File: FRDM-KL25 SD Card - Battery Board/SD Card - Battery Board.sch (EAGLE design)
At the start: 16 parts, among them U1 TPS63001, U2 TPS63002

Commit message: FRDM-KL25Z: Changed library used for passives
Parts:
- R1, R2, R3, R4, R5, R6, R7, R8: device Kas-Passives:RESISTOR10K-62.5M-1%-50V -> Kas-Resistors:RESISTOR10K-62.5M-1%-50V
- R10, R9: device Kas-Passives:RESISTOR0402 -> Kas-Resistors:RESISTOR200-100M-1%-50V
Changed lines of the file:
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@@
 <part name="U$1" library="Kas-Connectors" deviceset="693061010991" device=""/>
 <part name="C1" library="Kas-Passives" deviceset="CAPACITOR" device="1U-X5R-10%-10V" value="1 uF"/>
-<part name="R1" library="Kas-Passives" deviceset="RESISTOR" device="10K-62.5M-1%-50V" value="10k"/>
-<part name="R2" library="Kas-Passives" deviceset="RESISTOR" device="10K-62.5M-1%-50V" value="10k"/>
-<part name="R3" library="Kas-Passives" deviceset="RESISTOR" device="10K-62.5M-1%-50V" value="10k"/>
-<part name="R4" library="Kas-Passives" deviceset="RESISTOR" device="10K-62.5M-1%-50V" value="10k"/>
-<part name="R5" library="Kas-Passives" deviceset="RESISTOR" device="10K-62.5M-1%-50V" value="10k"/>
-<part name="R6" library="Kas-Passives" deviceset="RESISTOR" device="10K-62.5M-1%-50V" value="10k"/>
-<part name="R7" library="Kas-Passives" deviceset="RESISTOR" device="10K-62.5M-1%-50V" value="10k"/>
-<part name="R8" library="Kas-Passives" deviceset="RESISTOR" device="10K-62.5M-1%-50V" value="10k"/>
-<part name="R9" library="Kas-Passives" deviceset="RESISTOR" device="0402" value="200"/>
-<part name="R10" library="Kas-Passives" deviceset="RESISTOR" device="0402" value="200"/>
+<part name="R1" library="Kas-Resistors" deviceset="RESISTOR" device="10K-62.5M-1%-50V" value="10k"/>
+<part name="R2" library="Kas-Resistors" deviceset="RESISTOR" device="10K-62.5M-1%-50V" value="10k"/>
+<part name="R3" library="Kas-Resistors" deviceset="RESISTOR" device="10K-62.5M-1%-50V" value="10k"/>
+<part name="R4" library="Kas-Resistors" deviceset="RESISTOR" device="10K-62.5M-1%-50V" value="10k"/>
+<part name="R5" library="Kas-Resistors" deviceset="RESISTOR" device="10K-62.5M-1%-50V" value="10k"/>
+<part name="R6" library="Kas-Resistors" deviceset="RESISTOR" device="10K-62.5M-1%-50V" value="10k"/>
+<part name="R7" library="Kas-Resistors" deviceset="RESISTOR" device="10K-62.5M-1%-50V" value="10k"/>
+<part name="R8" library="Kas-Resistors" deviceset="RESISTOR" device="10K-62.5M-1%-50V" value="10k"/>
+<part name="R9" library="Kas-Resistors" deviceset="RESISTOR" device="200-100M-1%-50V" value="200"/>
+<part name="R10" library="Kas-Resistors" deviceset="RESISTOR" device="200-100M-1%-50V" value="200"/>
 <part name="U1" library="Kas-Buck Boost Battery Control" deviceset="TPS6300X" device="" value="TPS63001"/>
 <part name="U2" library="Kas-Buck Boost Battery Control" deviceset="TPS6300X" device="" value="TPS63002"/>

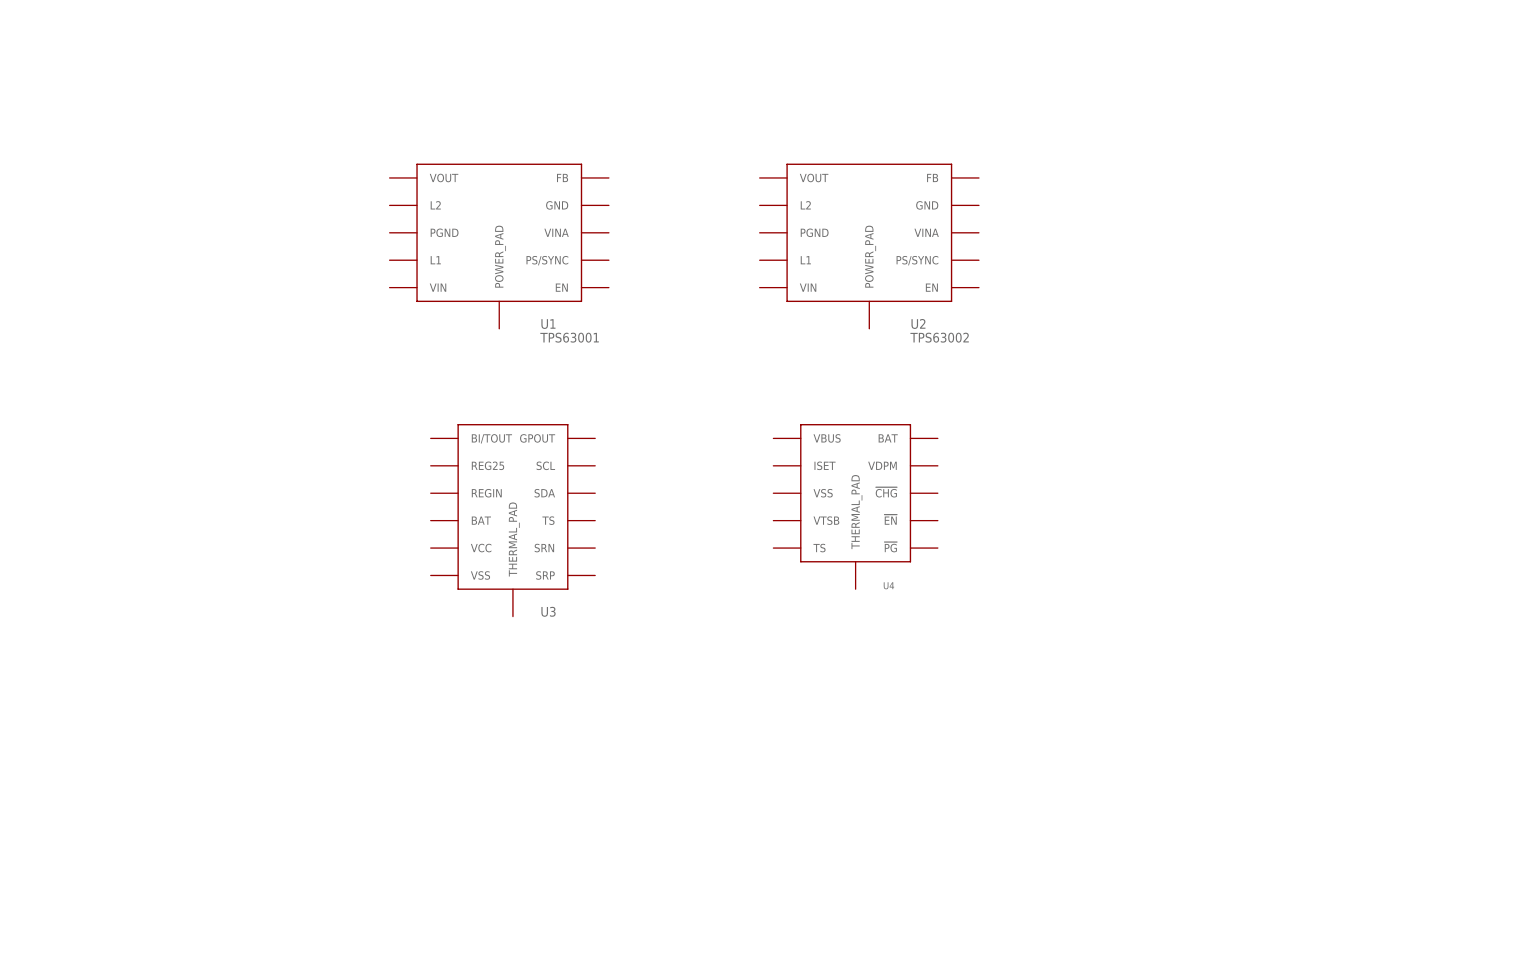
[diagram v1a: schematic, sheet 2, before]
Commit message: Removed .epf from version control, updated components
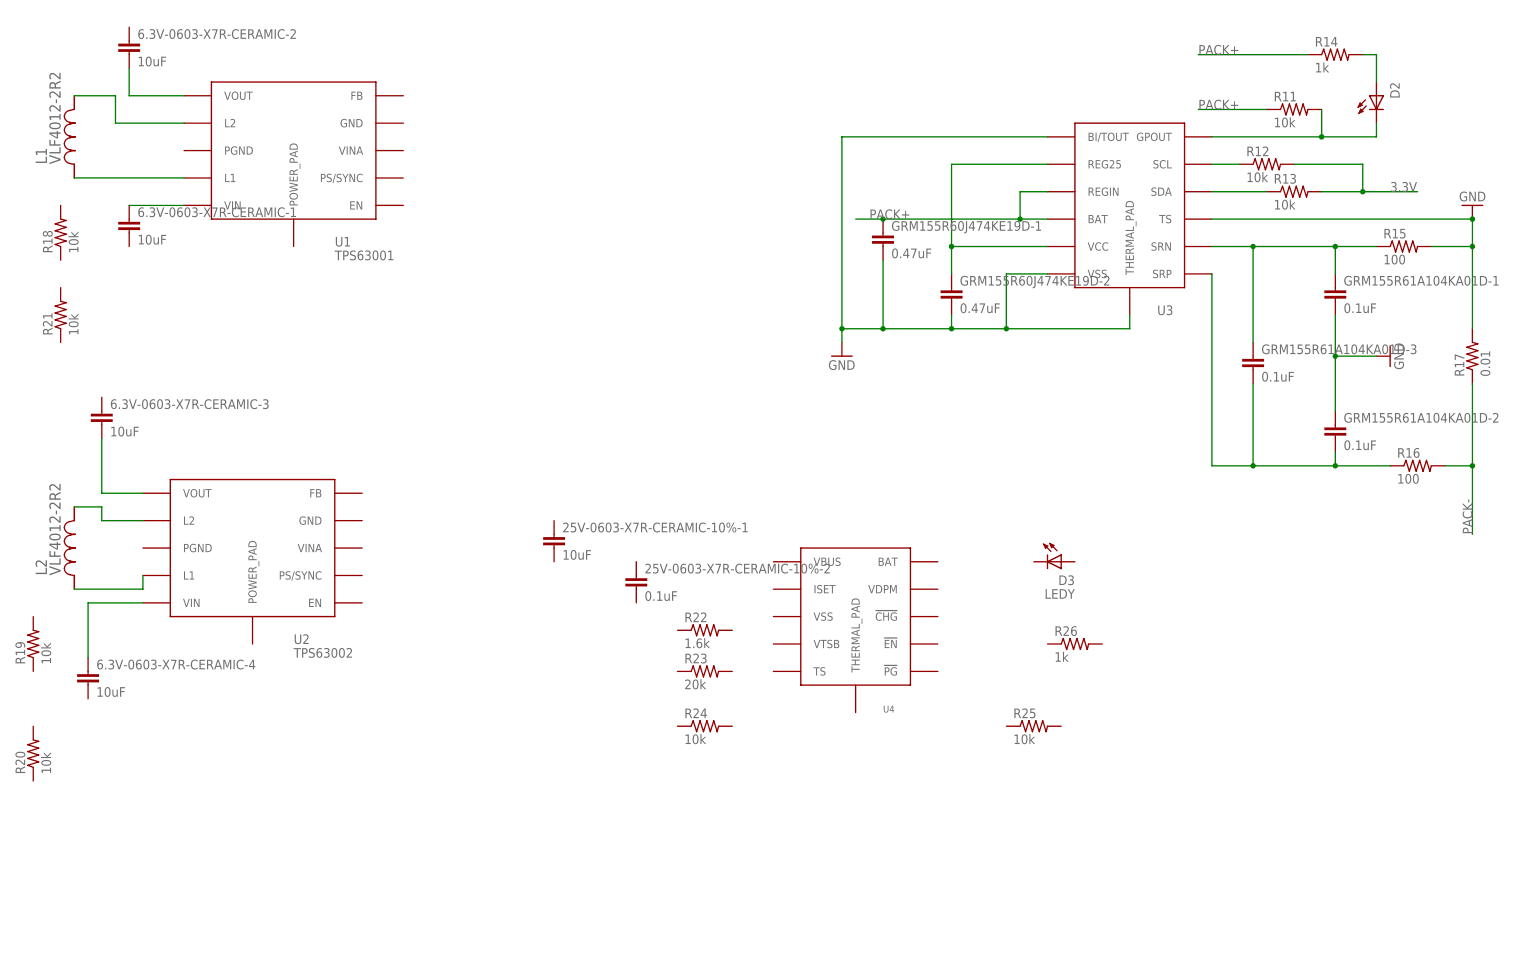
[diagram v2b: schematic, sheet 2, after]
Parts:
- removed U$1: 693061010991, Kas-Connectors:693061010991
- added 25V-0603-X7R-CERAMIC-10%-1, 6.3V-0603-X7R-CERAMIC-1, 6.3V-0603-X7R-CERAMIC-2, 6.3V-0603-X7R-CERAMIC-3, 6.3V-0603-X7R-CERAMIC-4: 10uF, Kas-Capacitors:CAPACITOR0603
- added 25V-0603-X7R-CERAMIC-10%-2, GRM155R61A104KA01D-1, GRM155R61A104KA01D-2, GRM155R61A104KA01D-3: 0.1uF, Kas-Capacitors:CAPACITOR0603
- added D2: (no value), Kas-Diodes-LEDs:LEDR
- added D3: LEDY, Kas-Diodes-LEDs:LEDG
- added GRM155R60J474KE19D-1, GRM155R60J474KE19D-2: 0.47uF, Kas-Capacitors:CAPACITOR0603
- added J1: (no value), Kas-Connectors:SD_CARD_SLOT
- added L1, L2: VLF4012-2R2, Kas-Inductors:XAL4020-222MEB
- added R11, R12, R13, R18, R19, R20, R21, R24, R25: 10k, Kas-Resistors:RESISTOR10K-62.5M-1%-50V
- added R14, R26: 1k, Kas-Resistors:RESISTOR0402
- added R15, R16: 100, Kas-Resistors:RESISTOR0402
- added R17: 0.01, Kas-Resistors:RESISTOR0402
- added R22: 1.6k, Kas-Resistors:RESISTOR0402
- added R23: 20k, Kas-Resistors:RESISTOR0402
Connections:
- new net 3.3V: R12.2, R13.2
- new net GND: GRM155R60J474KE19D-1.2, GRM155R60J474KE19D-2.2, GRM155R61A104KA01D-1.2, GRM155R61A104KA01D-2.1, R15.2, R17.2, U3.BI/TOUT, U3.THERMAL_PAD, U3.TS, U3.VSS
- new net N$1: GRM155R60J474KE19D-2.1, U3.REG25, U3.VCC
- new net N$10: 6.3V-0603-X7R-CERAMIC-1.1, U1.VIN
- new net N$11: 6.3V-0603-X7R-CERAMIC-2.2, U1.VOUT
- new net N$12: 6.3V-0603-X7R-CERAMIC-4.1, U2.VIN
- new net N$13: 6.3V-0603-X7R-CERAMIC-3.2, U2.VOUT
- new net N$14: L2.1, U2.L2
- new net N$15: L2.2, U2.L1
- new net N$2: R12.1, U3.SCL
- new net N$3: R13.1, U3.SDA
- new net N$4: D2.C, R11.2, U3.GPOUT
- new net N$5: D2.A, R14.2
- new net N$6: GRM155R61A104KA01D-2.2, GRM155R61A104KA01D-3.2, R16.1, U3.SRP
- new net N$7: GRM155R61A104KA01D-1.1, GRM155R61A104KA01D-3.1, R15.1, U3.SRN
- new net N$8: L1.1, U1.L2
- new net N$9: L1.2, U1.L1
- new net PACK+: GRM155R60J474KE19D-1.1, R11.1, R14.1, U3.BAT, U3.REGIN
- new net PACK-: R16.2, R17.1
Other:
- note added: "add schottky diode"
- moved on the sheet: U1, U2, U3, U4

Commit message: FRDM-KL25Z: Changed passives to use Newark approved parts
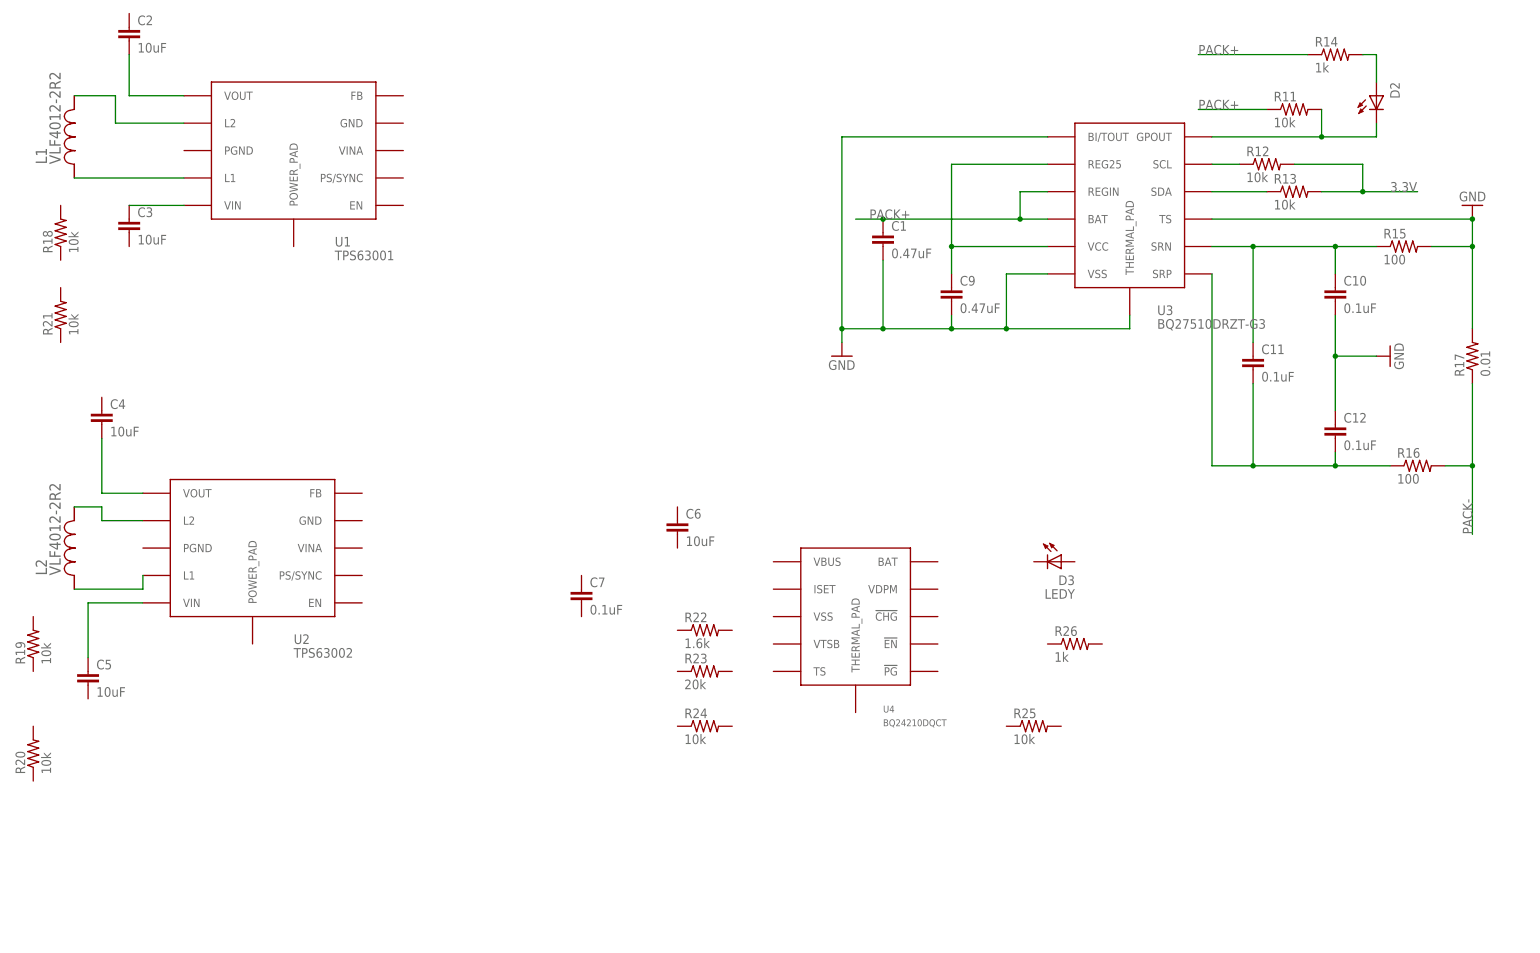
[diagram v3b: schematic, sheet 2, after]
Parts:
- removed 25V-0603-X7R-CERAMIC-10%-1, 6.3V-0603-X7R-CERAMIC-1, 6.3V-0603-X7R-CERAMIC-2, 6.3V-0603-X7R-CERAMIC-3, 6.3V-0603-X7R-CERAMIC-4: 10uF, Kas-Capacitors:CAPACITOR0603
- removed 25V-0603-X7R-CERAMIC-10%-2, GRM155R61A104KA01D-1, GRM155R61A104KA01D-2, GRM155R61A104KA01D-3: 0.1uF, Kas-Capacitors:CAPACITOR0603
- removed GRM155R60J474KE19D-1, GRM155R60J474KE19D-2: 0.47uF, Kas-Capacitors:CAPACITOR0603
- added C10, C11, C12, C7: 0.1uF, Kas-Capacitors:CAPACITOR0.1U-X5R-10%-10V-0402
- added C2, C3, C4, C5: 10uF, Kas-Capacitors:CAPACITOR10U-X7R-10%-6.3V
- added C6: 10uF, Kas-Capacitors:CAPACITOR10U-X7R-10%-25
- added C8: 1uF, Kas-Capacitors:CAPACITOR0.1U-X5R-10%-10V-0402
- added C9: 0.47uF, Kas-Capacitors:CAPACITOR0.1U-X5R-10%-10V-0402
- C1: value 1 uF -> 0.47uF; device Kas-Passives:CAPACITOR1U-X5R-10%-10V -> Kas-Capacitors:CAPACITOR0.1U-X5R-10%-10V-0402
- R10, R9: device Kas-Resistors:RESISTOR200-100M-1%-50V -> Kas-Resistors:RESISTOR0-100M-X%-50V
- R14, R15, R16, R17, R22, R23: device Kas-Resistors:RESISTOR0402 -> Kas-Resistors:RESISTOR0-100M-X%-50V
- R26: device Kas-Resistors:RESISTOR0402 -> Kas-Resistors:RESISTOR1K-62.5M-0.1%-75V
- U1: device Kas-Buck Boost Battery Control:TPS6300X -> Kas-Buck Boost Battery Control:TPS6300XTPS63001
- U2: device Kas-Buck Boost Battery Control:TPS6300X -> Kas-Buck Boost Battery Control:TPS6300XTPS63002
- U3: value (none) -> BQ27510DRZT-G3
- U4: value (none) -> BQ24210DQCT
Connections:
- net GND: now also C1.2, C10.2, C12.1, C9.2; no longer GRM155R60J474KE19D-1.2, GRM155R60J474KE19D-2.2, GRM155R61A104KA01D-1.2, GRM155R61A104KA01D-2.1
- net N$1: now also C9.1; no longer GRM155R60J474KE19D-2.1
- net N$10: now also C3.1; no longer 6.3V-0603-X7R-CERAMIC-1.1
- net N$11: now also C2.2; no longer 6.3V-0603-X7R-CERAMIC-2.2
- net N$12: now also C5.1; no longer 6.3V-0603-X7R-CERAMIC-4.1
- net N$13: now also C4.2; no longer 6.3V-0603-X7R-CERAMIC-3.2
- net N$6: now also C11.2, C12.2; no longer GRM155R61A104KA01D-2.2, GRM155R61A104KA01D-3.2
- net N$7: now also C10.1, C11.1; no longer GRM155R61A104KA01D-1.1, GRM155R61A104KA01D-3.1
- net PACK+: now also C1.1; no longer GRM155R60J474KE19D-1.1
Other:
- note removed: "Change to 0603 Capacitor"

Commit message: FRDM-KL25Z: Corrected parts to use Newark approved components and added missing componnets
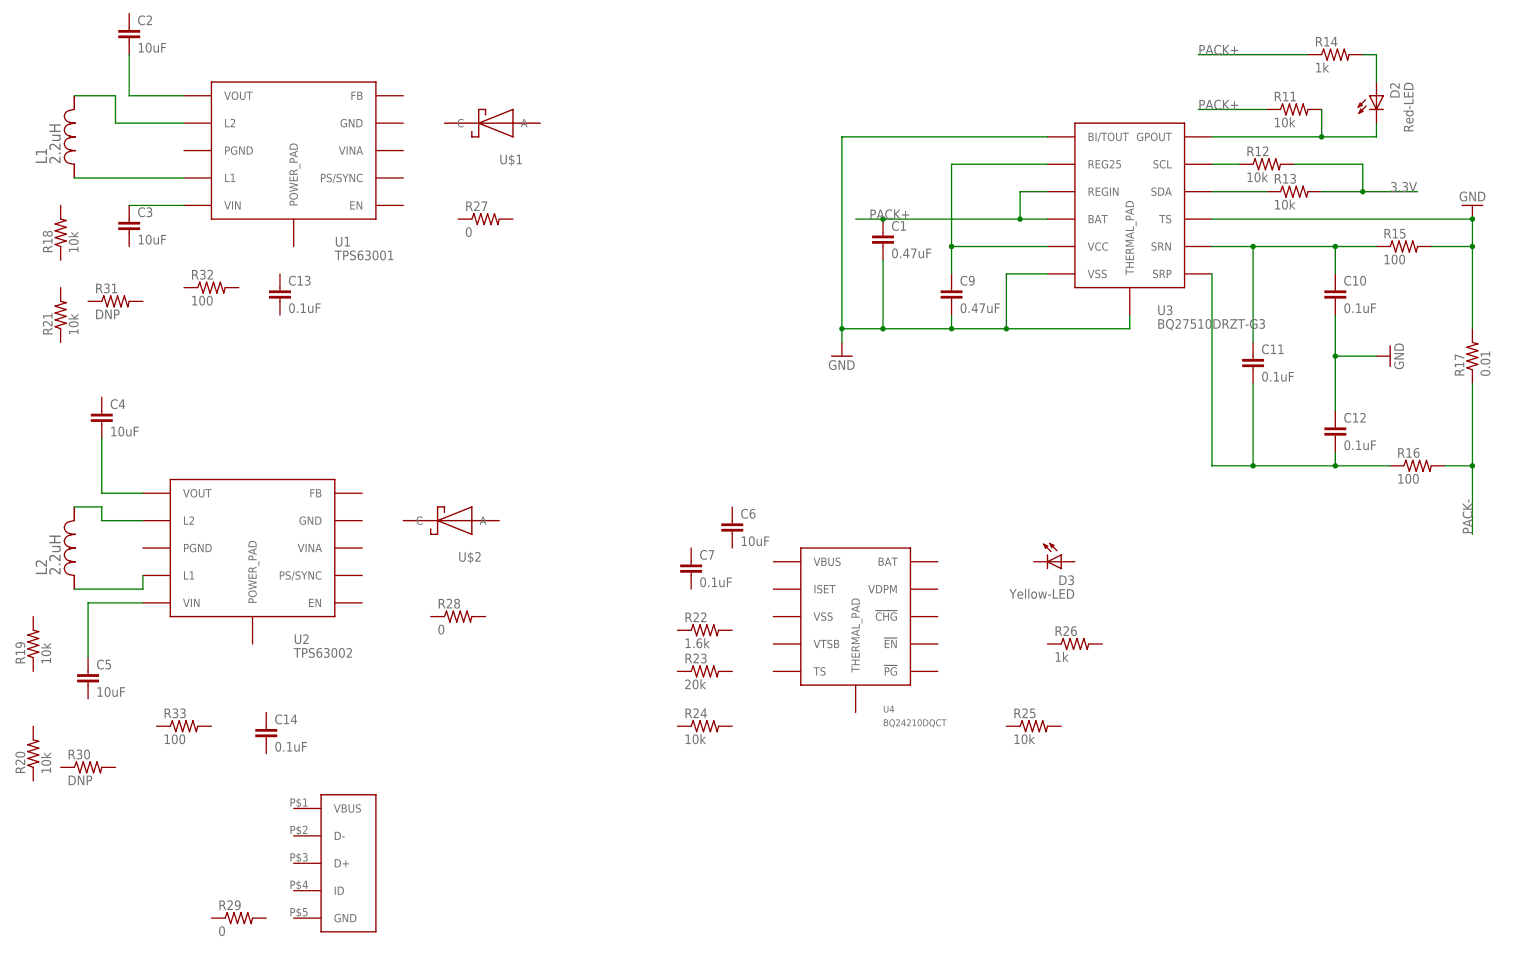
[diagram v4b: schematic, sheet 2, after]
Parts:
- added C13, C14: 0.1uF, Kas-Capacitors:CAPACITOR0.1U-X7R-10%-10V
- added R27, R28, R29: 0, Kas-Resistors:RESISTOR0-100M-X%-50V
- added R30, R31: DNP, Kas-Resistors:RESISTOR0603
- added R32, R33: 100, Kas-Resistors:RESISTOR100-62.5M-0.1%-75V
- added U$1, U$2: (no value), Kas-Diodes-LEDs:SCHOTTKY
- added U$3: (no value), Kas-Connectors:USB-MICROSD-47346-001
- C1, C9: device Kas-Capacitors:CAPACITOR0.1U-X5R-10%-10V-0402 -> Kas-Capacitors:CAPACITOR0.47U-X5R-10%-6.3V-0603
- C10, C11, C12: device Kas-Capacitors:CAPACITOR0.1U-X5R-10%-10V-0402 -> Kas-Capacitors:CAPACITOR0.1U-X5R-10%25V-0603
- C7: device Kas-Capacitors:CAPACITOR0.1U-X5R-10%-10V-0402 -> Kas-Capacitors:CAPACITOR0.1U-X7R-10%-25V
- C8: device Kas-Capacitors:CAPACITOR0.1U-X5R-10%-10V-0402 -> Kas-Capacitors:CAPACITOR1U-X5R-10%-10V-0603
- D2: value (none) -> Red-LED; device Kas-Diodes-LEDs:LEDR -> Kas-Diodes-LEDs:1.6X3.2R-1.85V-20MA
- D3: value LEDY -> Yellow-LED; device Kas-Diodes-LEDs:LEDG -> Kas-Diodes-LEDs:1.6X3.2Y-X.XX-XXMA
- L1, L2: value VLF4012-2R2 -> 2.2uH; device Kas-Inductors:XAL4020-222MEB -> Kas-Inductors:TY0NRS4010T2R2MDGG
- R1, R11, R12, R13, R18, R19, R2, R20, R21, R24, R25, R3, R4, R5, R6, R7, R8: device Kas-Resistors:RESISTOR10K-62.5M-1%-50V -> Kas-Resistors:RESISTOR10K-63M-1%-50V
- R10, R9: device Kas-Resistors:RESISTOR0-100M-X%-50V -> Kas-Resistors:RESISTOR200-100M-0.1%-75V
- R14: device Kas-Resistors:RESISTOR0-100M-X%-50V -> Kas-Resistors:RESISTOR1K-62.5M-0.1%-75V
- R15, R16: device Kas-Resistors:RESISTOR0-100M-X%-50V -> Kas-Resistors:RESISTOR100-62.5M-0.1%-75V
- R22: device Kas-Resistors:RESISTOR0-100M-X%-50V -> Kas-Resistors:RESISTOR1.6K-125M-0.1%-100V
- R23: device Kas-Resistors:RESISTOR0-100M-X%-50V -> Kas-Resistors:RESISTOR20K-63M-1%-50V
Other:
- note removed: "Change to 0603 Resistors"
- note removed: "add schottky diode"
- moved on the sheet: C6, C7
